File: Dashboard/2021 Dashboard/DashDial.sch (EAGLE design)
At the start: 30 parts, among them IC2 TLC5952DAP, J1 ESW-104-23-L-D, J2 ESW-104-23-L-D

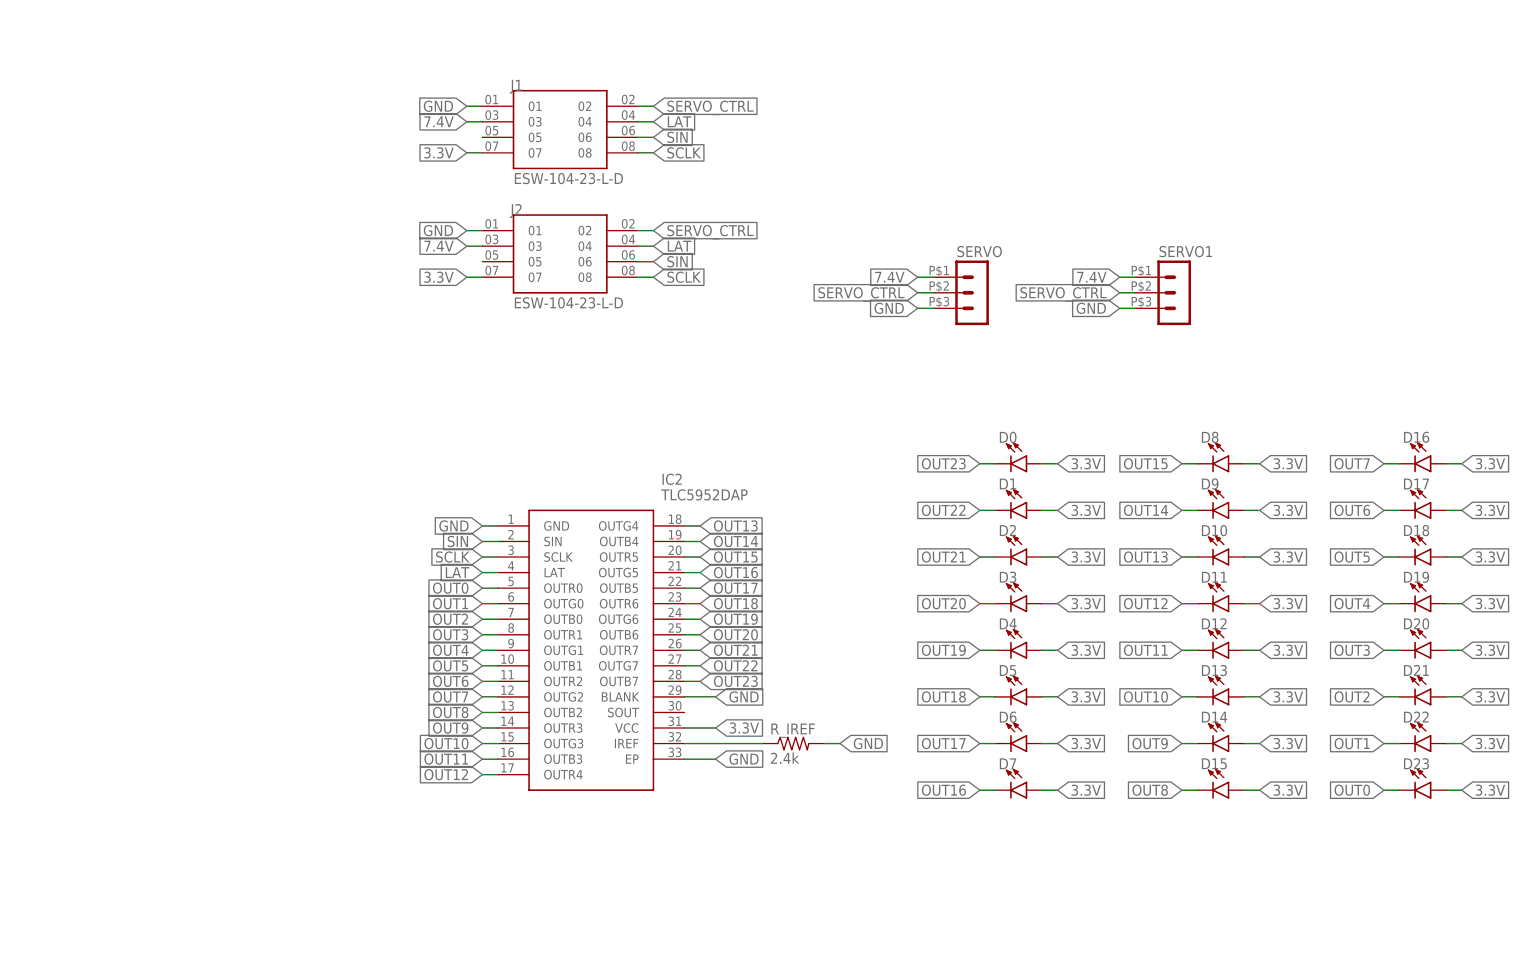
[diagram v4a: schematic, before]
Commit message: Updated all dashboard stuff
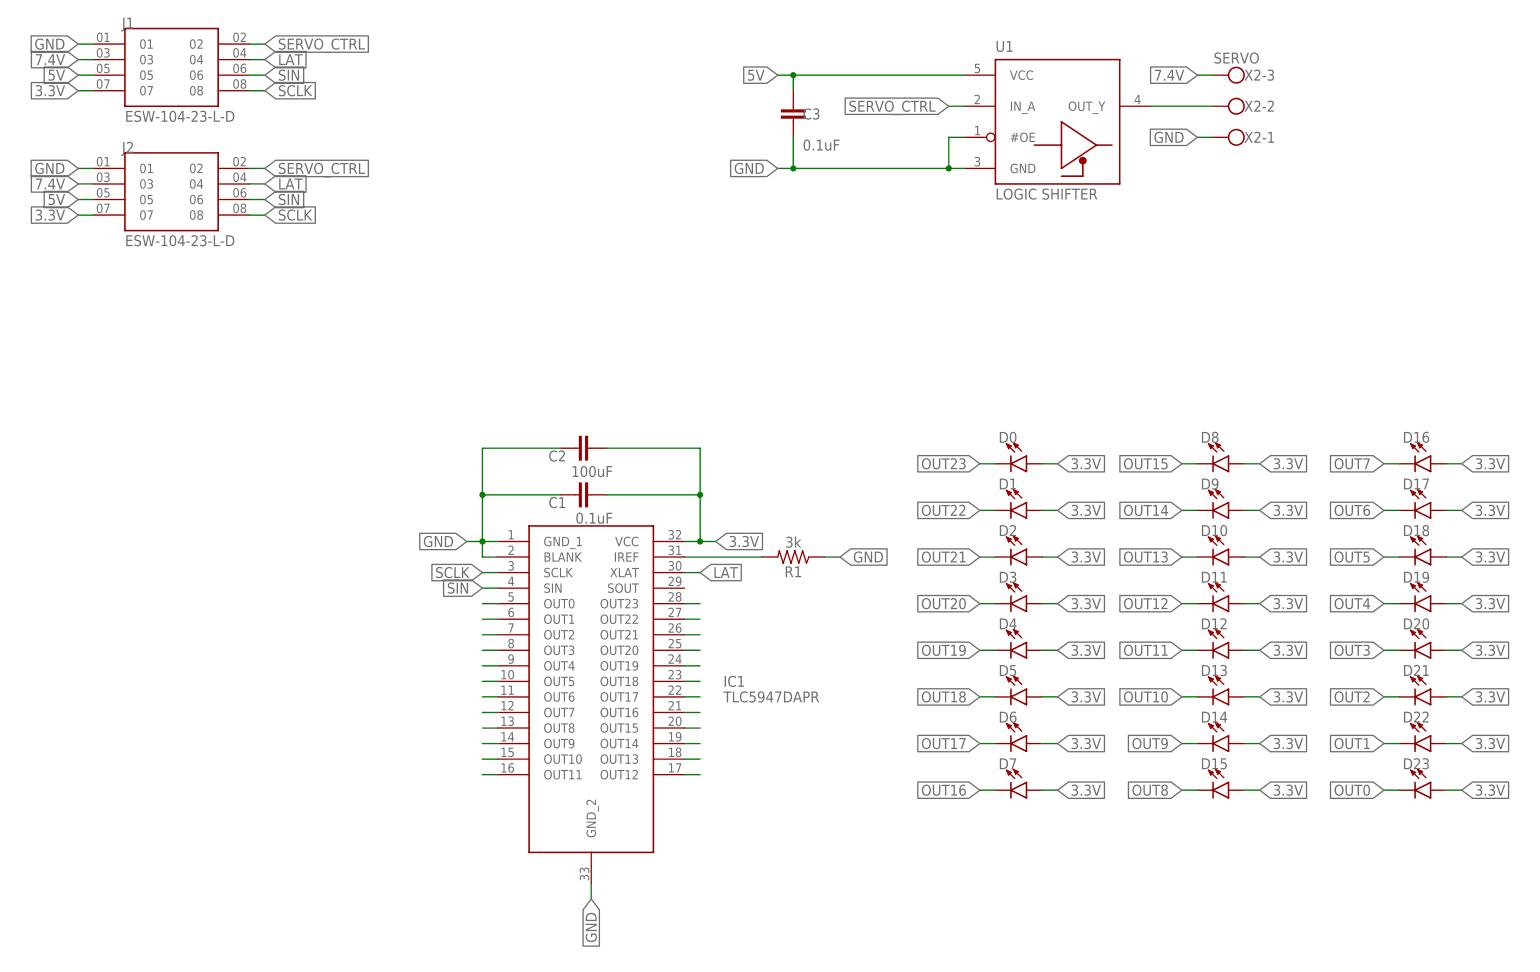
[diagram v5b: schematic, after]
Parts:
- removed IC2: TLC5952DAP, GTOR - Active Components:TLC5952DAP
- removed R_IREF: 2.4k, GTOR - Passive Components:RES_SMDR0603
- removed SERVO, SERVO1: (no value), GTOR - Microfit Connector:HEADER_POS3_43650-0300
- added C1: 0.1uF, rcl:C-EUC0402
- added C2: 100uF, rcl:C-EUC1206
- added C3: 0.1uF, SparkFun-Capacitors:0.1UF-0603-25V-(+80/-20%)
- added IC1: TLC5947DAPR, TLC5947DAPR:TLC5947DAPR
- added R1: 3k, SparkFun-Resistors:RESISTORAXIAL-0.3
- added U1: LOGIC SHIFTER, MC74VHC1GT125:MC74VHC1GT125DF
- added X2: SERVO, con-wago-500:W237-103
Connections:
- removed net N$31: IC2.IREF, R_IREF.1
- new net 5V: C3.1, J1.05, J2.05, U1.VCC
- new net N$1: U1.OUT_Y, X2-2.KL
- new net N$32: IC1.IREF, R1.2
- net 3.3V: now also C1.2, C2.2, IC1.VCC; no longer IC2.VCC
- net 7.4V: now also X2-3.KL; no longer SERVO.1, SERVO1.1
- net GND: now also C1.1, C2.1, C3.2, IC1.BLANK, IC1.GND_1, IC1.GND_2, R1.1, U1.#OE, U1.GND, X2-1.KL; no longer IC2.BLANK, IC2.EP, IC2.GND, R_IREF.2, SERVO.3, SERVO1.3
- net LAT: now also IC1.XLAT; no longer IC2.LAT
- net OUT0: now also IC1.OUT0; no longer IC2.OUTR0
- net OUT1: now also IC1.OUT1; no longer IC2.OUTG0
- net OUT10: now also IC1.OUT10; no longer IC2.OUTG3
- net OUT11: now also IC1.OUT11; no longer IC2.OUTB3
- net OUT12: now also IC1.OUT12; no longer IC2.OUTR4
- net OUT13: now also IC1.OUT13; no longer IC2.OUTG4
- net OUT14: now also IC1.OUT14; no longer IC2.OUTB4
- net OUT15: now also IC1.OUT15; no longer IC2.OUTR5
- net OUT16: now also IC1.OUT16; no longer IC2.OUTG5
- net OUT17: now also IC1.OUT17; no longer IC2.OUTB5
- net OUT18: now also IC1.OUT18; no longer IC2.OUTR6
- net OUT19: now also IC1.OUT19; no longer IC2.OUTG6
- net OUT2: now also IC1.OUT2; no longer IC2.OUTB0
- net OUT20: now also IC1.OUT20; no longer IC2.OUTB6
- net OUT21: now also IC1.OUT21; no longer IC2.OUTR7
- net OUT22: now also IC1.OUT22; no longer IC2.OUTG7
- net OUT23: now also IC1.OUT23; no longer IC2.OUTB7
- net OUT3: now also IC1.OUT3; no longer IC2.OUTR1
- net OUT4: now also IC1.OUT4; no longer IC2.OUTG1
- net OUT5: now also IC1.OUT5; no longer IC2.OUTB1
- net OUT6: now also IC1.OUT6; no longer IC2.OUTR2
- net OUT7: now also IC1.OUT7; no longer IC2.OUTG2
- net OUT8: now also IC1.OUT8; no longer IC2.OUTB2
- net OUT9: now also IC1.OUT9; no longer IC2.OUTR3
- net SCLK: now also IC1.SCLK; no longer IC2.SCLK
- net SERVO_CTRL: now also U1.IN_A; no longer SERVO.2, SERVO1.2
- net SIN: now also IC1.SIN; no longer IC2.SIN
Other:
- note added: "DashDial V2 Designer: Akash Harapanahalli"
- note removed: "DashDial V3 Designer: Param Pithadia"
- moved on the sheet: J1, J2
